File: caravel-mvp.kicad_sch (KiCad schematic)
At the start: 46 parts, among them J2 Conn_01x02, J3 Conn_02x04_Odd_Even, J4 Conn_01x06, J6 Conn_02x18_Odd_Even, J6 USB_C_Receptacle_USB2.0, J9 613012243121, SW3 B3U-1000P, U1 Caravel_QFN_TT3, U1 W25Q32JVSS, X1 10MHz

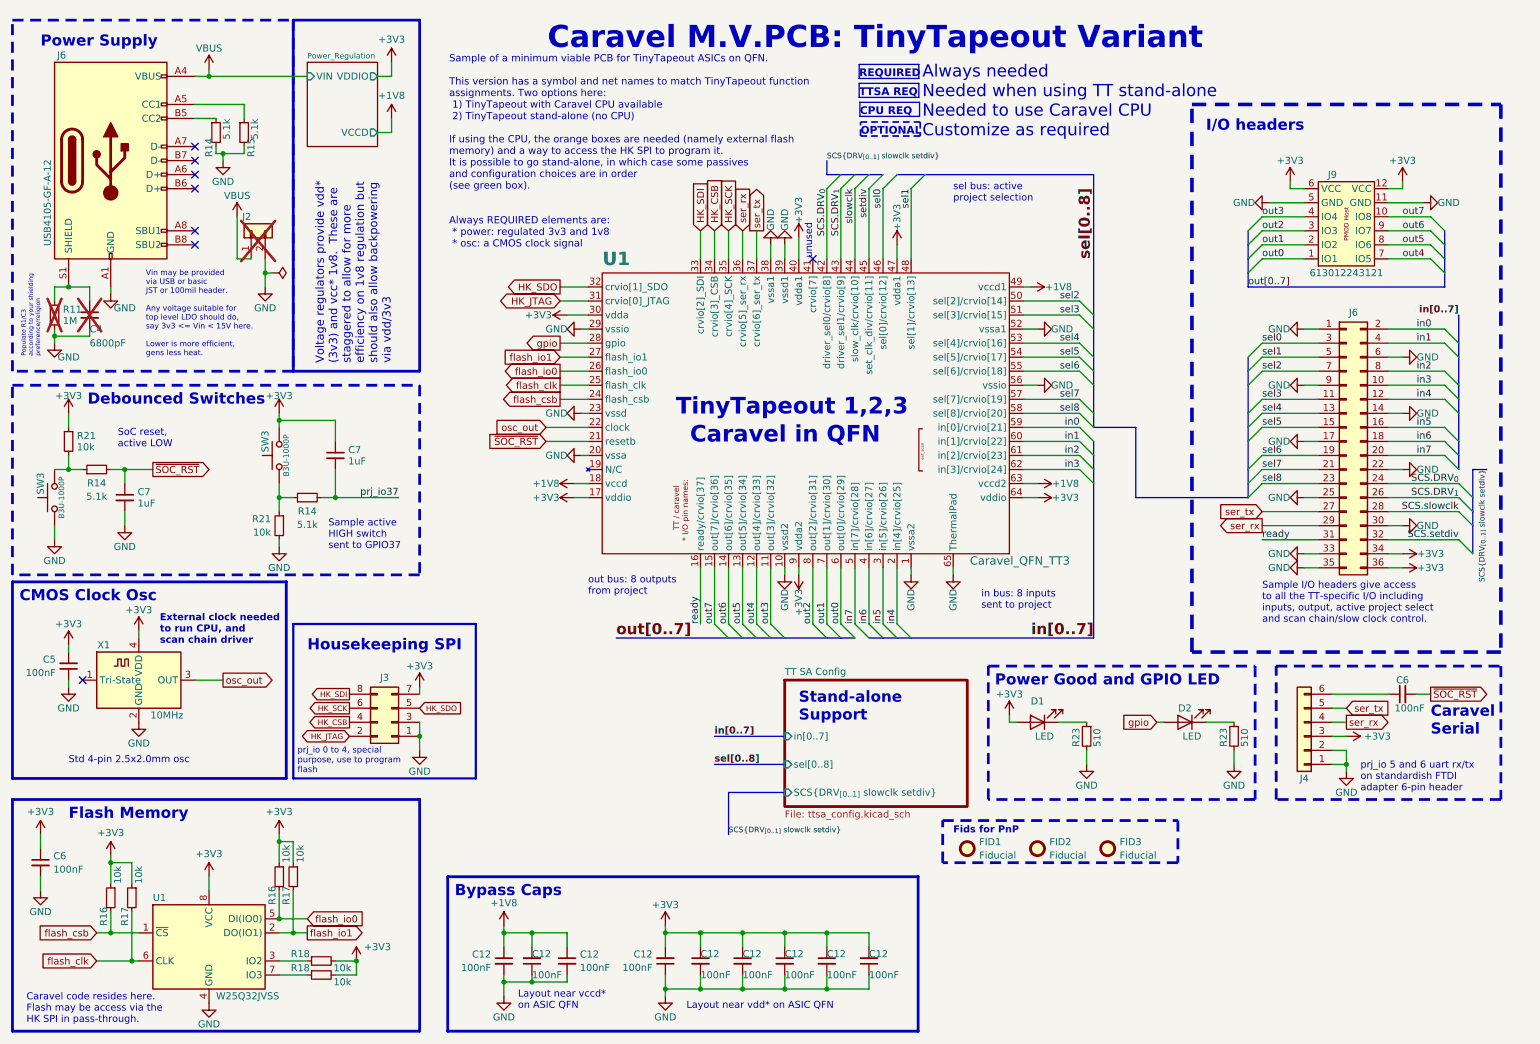
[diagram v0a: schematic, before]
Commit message: Reset rise and slow clock config fixes
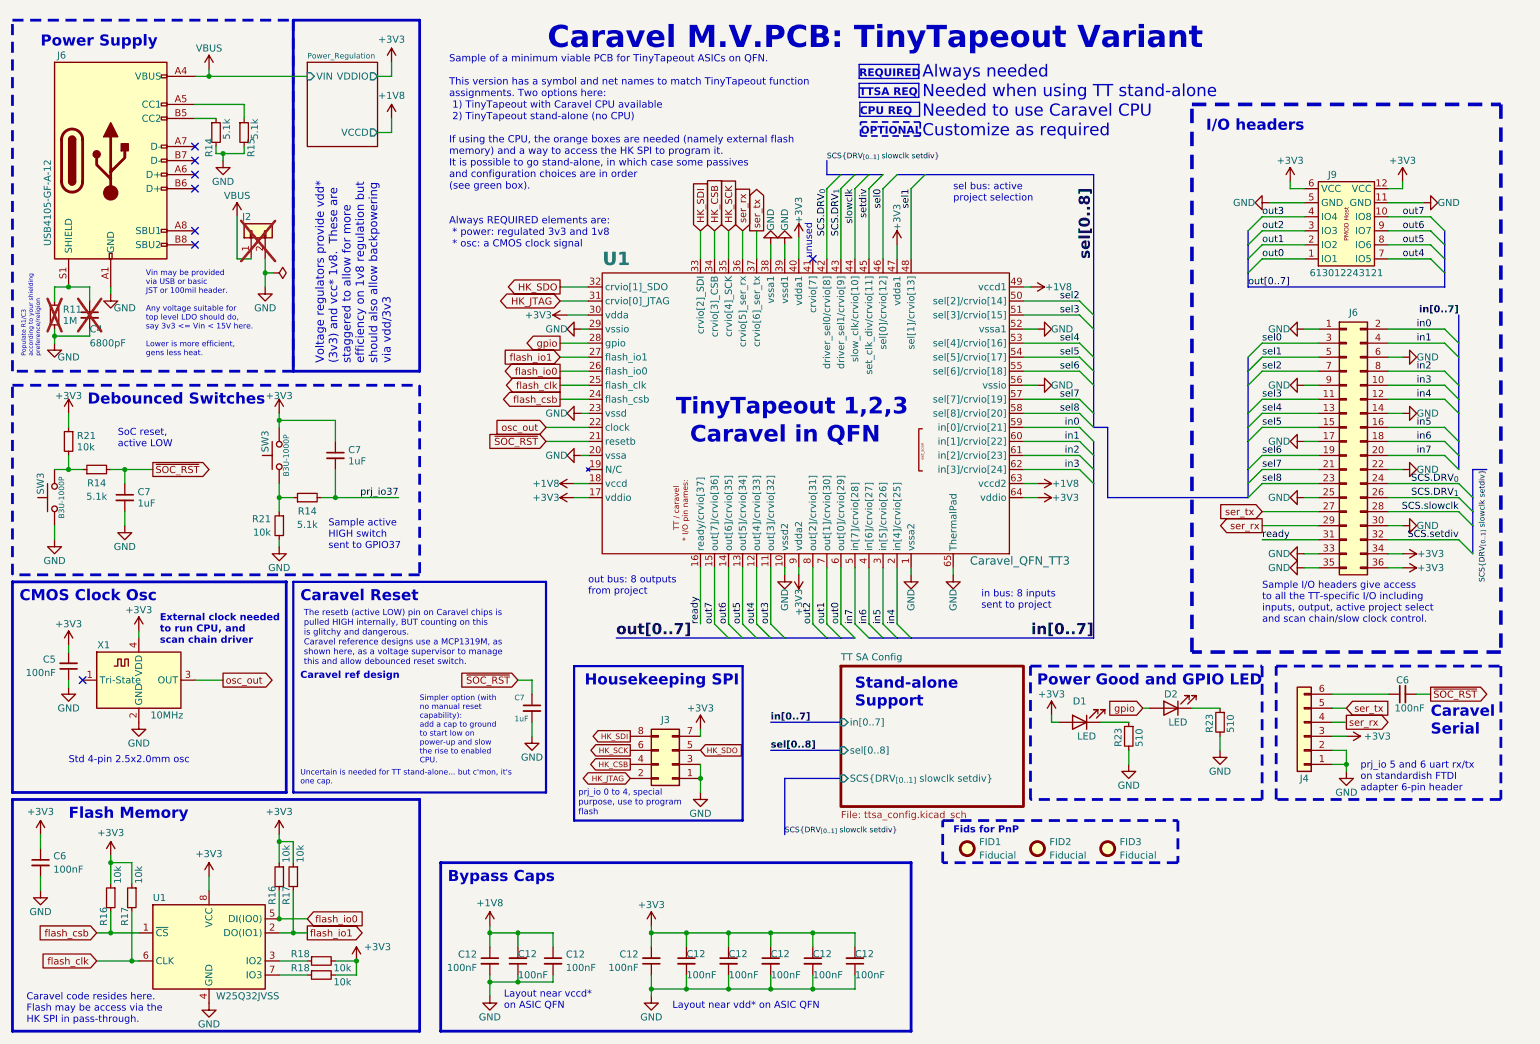
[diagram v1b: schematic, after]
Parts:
- added C7: 1uF, Capacitor_SMD:C_0603_1608Metric, symbol Device:C_Small
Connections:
- net GND: now also C7.2
- net ~{SOC_RST}: now also C7.1
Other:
- note added: "Caravel Reset"
- note added: "Caravel ref design"
- note added: "Simpler option (with no manual reset capability): add a cap to ground to start low on power-up and slow the rise to enabled CPU."
- note added: "The resetb (active LOW) pin on Caravel chips is pulled HIGH internally, BUT counting on this is glitchy and dangerous. Caravel reference designs use a MCP1319M, as shown here, as a voltage supervisor to manage this and allow debounced reset switch."
- note added: "Uncertain is needed for TT stand-alone... but c'mon, it's one cap."
- moved on the sheet: C12, D1, D2, J3, R23

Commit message: Commenting and colour adjustments
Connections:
- net prj_io37 is gone; now on net in2: C7.2, R14.2
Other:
- note added: "Always needed"
- note added: "Customize as required"
- note added: "JTAG conn optional"
- note added: "Needed to use Caravel CPU"
- note added: "Needed when using TT stand-alone"
- note added: "Sample active HIGH switch sent to in2"
- note added: "Simpler option (with no manual reset capability): add a cap to ground to start low on power-up and slow the rise to enabled CPU. Only required if reset switch SW1 not present."
- note added: "TT Stand-alone Support"
- note removed: "Always needed Needed when using TT stand-alone Needed to use Caravel CPU Customize as required"
- note removed: "Sample active HIGH switch sent to GPIO37"
- note removed: "Simpler option (with no manual reset capability): add a cap to ground to start low on power-up and slow the rise to enabled CPU."
- note removed: "Stand-alone Support"
- note removed: "Uncertain is needed for TT stand-alone... but c'mon, it's one cap."

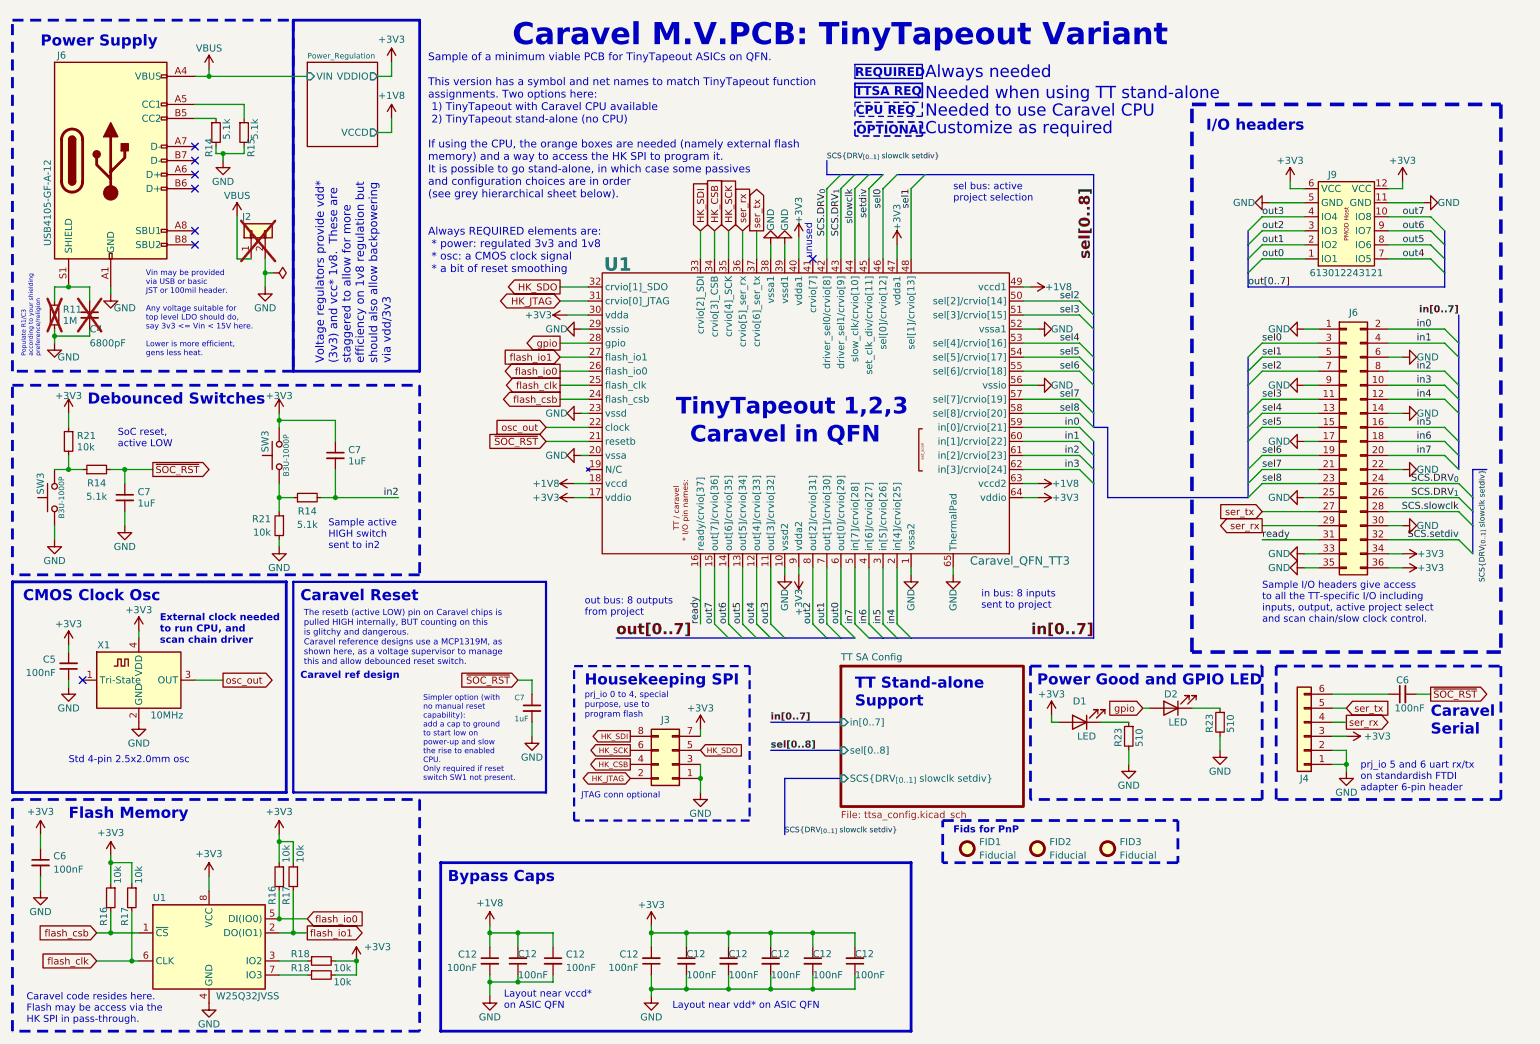
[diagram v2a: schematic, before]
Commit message: minor cleanups and clarifications
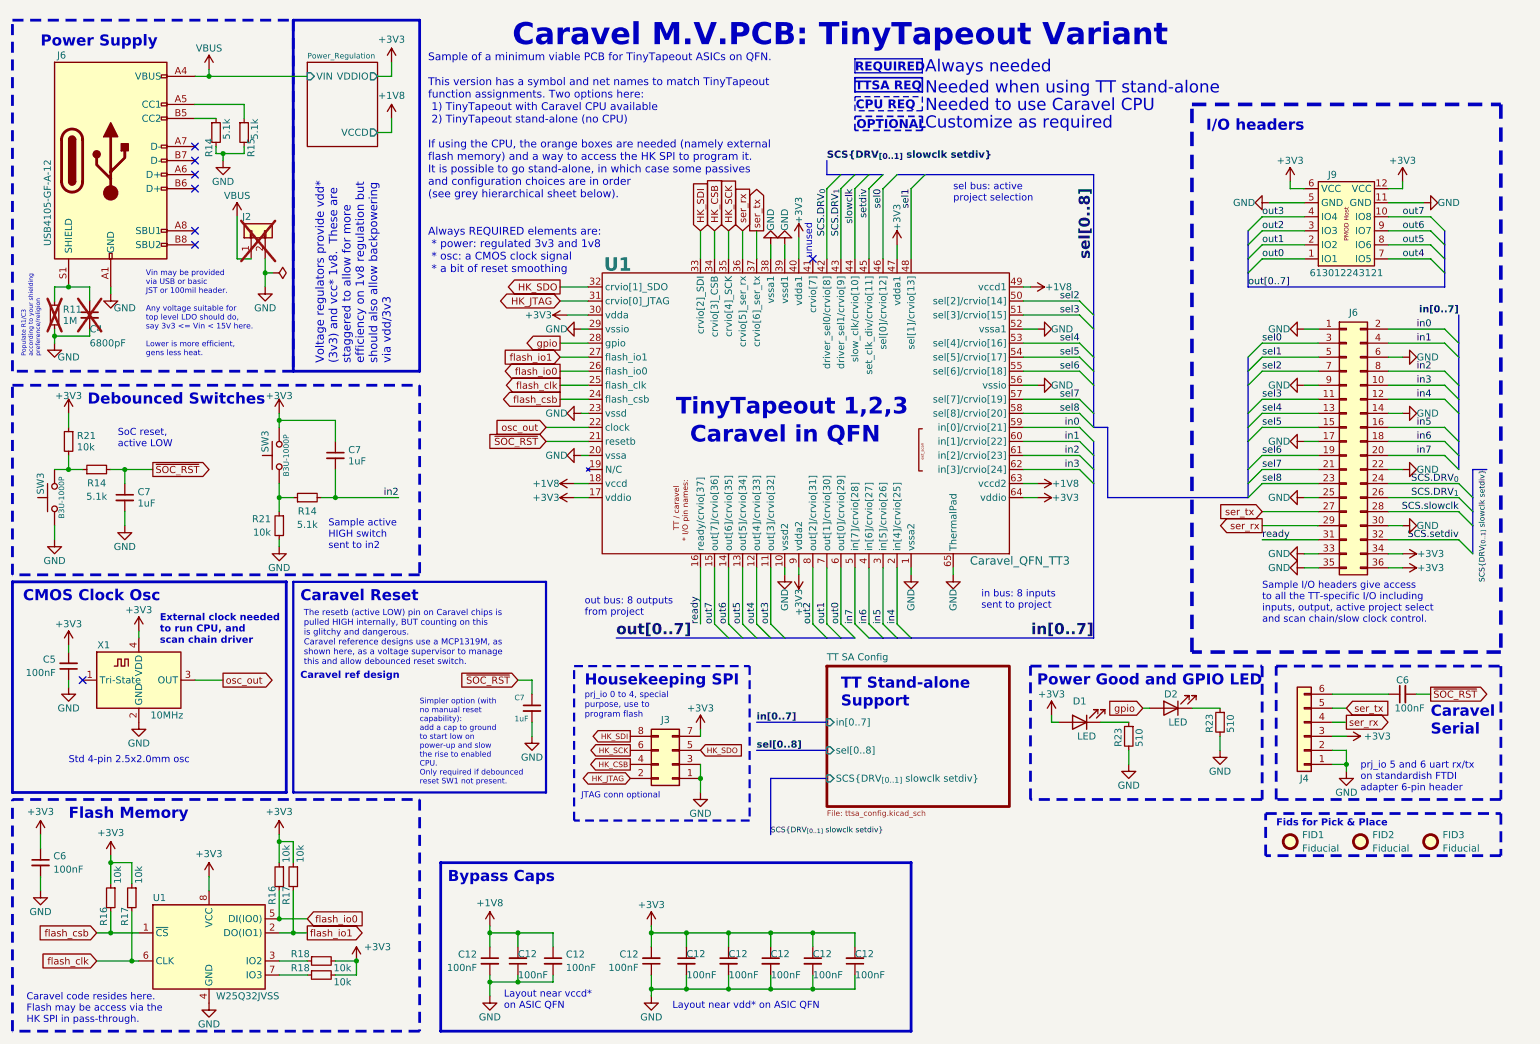
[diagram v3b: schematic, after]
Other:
- note added: "Fids for Pick & Place"
- note added: "Simpler option (with no manual reset capability): add a cap to ground to start low on power-up and slow the rise to enabled CPU. Only required if debounced reset SW1 not present."
- note removed: "Fids for PnP"
- note removed: "Simpler option (with no manual reset capability): add a cap to ground to start low on power-up and slow the rise to enabled CPU. Only required if reset switch SW1 not present."
- moved on the sheet: FID1, FID2, FID3
